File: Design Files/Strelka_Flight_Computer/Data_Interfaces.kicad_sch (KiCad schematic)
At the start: 9 parts, among them J2 Conn_01x04, J5 USB_B_Micro, J6 USB_B_Micro, U7 USBLC6-2SC6, U8 USBLC6-2SC6, U9 CP2102N-Axx-xQFN28

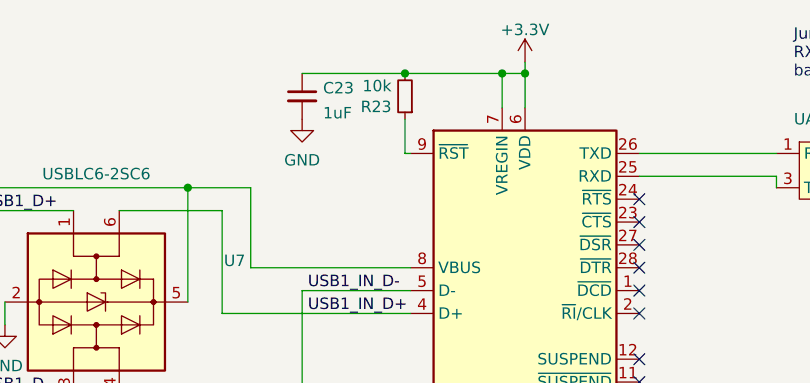
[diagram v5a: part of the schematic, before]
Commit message: Added motor driver to power board
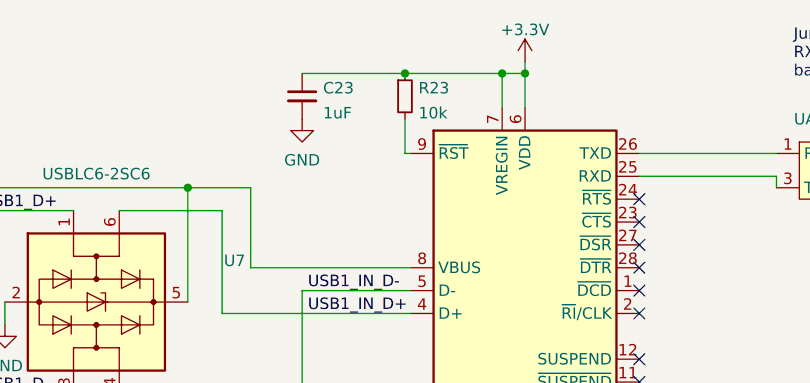
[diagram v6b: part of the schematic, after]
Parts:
- removed R23: 10k, Resistor_SMD:R_0603_1608Metric_Pad0.98x0.95mm_HandSolder, symbol Nebula-rescue:R_Small-Device-H7_FlightComputer-rescue
- added R23: 10k, Resistor_SMD:R_0603_1608Metric, symbol Device:R_Small
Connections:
- net +3V3: now also R23.1
- net at U9.9 (~{RST}): now also R23.2

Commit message: Creating BOM
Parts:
- removed J2: Conn_01x04, Connector_PinHeader_2.54mm:PinHeader_1x04_P2.54mm_Horizontal, symbol Connector_Generic:Conn_01x04
- added J2: SM04B-GHS-TB(LF)(SN)-, Footprints:JST_SM04B-GHS-TB(LF)(SN)-, symbol SM04B-GHS-TB_LF__SN_-:SM04B-GHS-TB(LF)(SN)-
- U7, U8: LCSC# (none) -> C2687116
- U9: LCSC# (none) -> C1550553
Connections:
- net +3V3: now also J2.4
- net GND: now also J2.3, J2.SH1 (SHIELD), J2.SH2 (SHIELD)
- net SWCLK: now also J2.1
- net SWDIO: now also J2.2
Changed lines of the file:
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@@
     (stroke (width 0) (type default) (color 0 0 0 0))
   )
-  (polyline (pts (xy 68.58 111.125) (xy 68.58 130.81))
+  (polyline (pts (xy 68.58 111.125) (xy 68.58 134.62))
     (stroke (width 0) (type default) (color 0 0 0 0))
   )
@@
     (stroke (width 0) (type default) (color 0 0 0 0))
   )
-  (wire (pts (xy 81.28 121.92) (xy 83.82 121.92))
+  (wire (pts (xy 77.47 121.92) (xy 83.82 121.92))
     (stroke (width 0) (type default) (color 0 0 0 0))
   )
@@
     (stroke (width 0) (type default) (color 0 0 0 0))
   )
-  (polyline (pts (xy 104.14 130.81) (xy 68.58 130.81))
+  (polyline (pts (xy 104.14 134.62) (xy 68.58 134.62))
     (stroke (width 0) (type default) (color 0 0 0 0))
   )
@@
     (stroke (width 0) (type default) (color 0 0 0 0))
   )
+  (wire (pts (xy 77.47 129.54) (xy 83.82 129.54))
+    (stroke (width 0) (type default) (color 0 0 0 0))
+  )
   (wire (pts (xy 212.09 30.48) (xy 222.885 30.48))
     (stroke (width 0) (type default) (color 0 0 0 0))
@@
     (stroke (width 0) (type default) (color 0 0 0 0))
   )
-  (wire (pts (xy 71.12 116.84) (xy 83.82 116.84))
-    (stroke (width 0) (type default) (color 0 0 0 0))
-  )
   (wire (pts (xy 187.96 85.09) (xy 187.96 97.79))
     (stroke (width 0) (type default) (color 0 0 0 0))
@@
     (stroke (width 0) (type default) (color 0 0 0 0))
   )
-  (polyline (pts (xy 104.14 111.125) (xy 104.14 130.81))
+  (polyline (pts (xy 104.14 111.125) (xy 104.14 134.62))
     (stroke (width 0) (type default) (color 0 0 0 0))
   )
@@
   )
   (wire (pts (xy 194.945 52.07) (xy 212.725 52.07))
+    (stroke (width 0) (type default) (color 0 0 0 0))
+  )
+  (wire (pts (xy 81.28 116.84) (xy 83.82 116.84))
     (stroke (width 0) (type default) (color 0 0 0 0))
   )
@@
     (effects (font (size 1.27 1.27)) (justify left bottom))
   )
-  (hierarchical_label "SWCLK" (shape input) (at 81.28 119.38 180)
+  (hierarchical_label "SWCLK" (shape input) (at 81.28 116.84 180)
     (effects (font (size 1.27 1.27)) (justify right))
   )
-  (hierarchical_label "SWDIO" (shape input) (at 81.28 121.92 180)
+  (hierarchical_label "SWDIO" (shape input) (at 81.28 119.38 180)
     (effects (font (size 1.27 1.27)) (justify right))
   )
@@
       (effects (font (size 1.27 1.27)) hide)
     )
+    (property "LCSC#" "C2687116" (id 4) (at 177.8 55.88 90)
+      (effects (font (size 1.27 1.27)) hide)
+    )
     (pin "1")
     (pin "2")
@@
     (pin "6")
   )
-  (symbol (lib_id "power:GND") (at 71.12 116.84 0) (unit 1)
+  (symbol (lib_id "power:GND") (at 77.47 121.92 0) (unit 1)
     (in_bom yes) (on_board yes)
-    (property "Reference" "#PWR0156" (id 0) (at 71.12 123.19 0)
-      (effects (font (size 1.27 1.27)) hide)
-    )
-    (property "Value" "GND" (id 1) (at 71.12 120.7676 0))
-    (property "Footprint" "" (id 2) (at 71.12 116.84 0)
-      (effects (font (size 1.27 1.27)) hide)
-    )
-    (property "Datasheet" "" (id 3) (at 71.12 116.84 0)
+    (property "Reference" "#PWR0156" (id 0) (at 77.47 128.27 0)
+      (effects (font (size 1.27 1.27)) hide)
+    )
+    (property "Value" "GND" (id 1) (at 77.47 125.8476 0))
+    (property "Footprint" "" (id 2) (at 77.47 121.92 0)
+      (effects (font (size 1.27 1.27)) hide)
+    )
+    (property "Datasheet" "" (id 3) (at 77.47 121.92 0)
       (effects (font (size 1.27 1.27)) hide)
     )
@@
     )
     (property "Datasheet" "" (id 3) (at 167.64 100.33 0)
+      (effects (font (size 1.27 1.27)) hide)
+    )
+    (pin "1")
+  )
+  (symbol (lib_id "power:GND") (at 77.47 129.54 0) (unit 1)
+    (in_bom yes) (on_board yes)
+    (property "Reference" "#PWR0112" (id 0) (at 77.47 135.89 0)
+      (effects (font (size 1.27 1.27)) hide)
+    )
+    (property "Value" "GND" (id 1) (at 77.47 133.4676 0))
+    (property "Footprint" "" (id 2) (at 77.47 129.54 0)
+      (effects (font (size 1.27 1.27)) hide)
+    )
+    (property "Datasheet" "" (id 3) (at 77.47 129.54 0)
       (effects (font (size 1.27 1.27)) hide)
     )
@@
       (effects (font (size 1.27 1.27)) hide)
     )
+    (property "LCSC#" "C2687116" (id 4) (at 177.8 97.79 90)
+      (effects (font (size 1.27 1.27)) hide)
+    )
     (pin "1")
     (pin "2")
@@
     (pin "6")
   )
-  (symbol (lib_id "Connector_Generic:Conn_01x04") (at 88.9 119.38 0) (unit 1)
-    (in_bom yes) (on_board yes) (fields_autoplaced)
-    (property "Reference" "J2" (id 0) (at 91.44 119.3799 0)
-      (effects (font (size 1.27 1.27)) (justify left))
-    )
-    (property "Value" "Conn_01x04" (id 1) (at 91.44 121.9199 0)
-      (effects (font (size 1.27 1.27)) (justify left))
-    )
-    (property "Footprint" "Connector_PinHeader_2.54mm:PinHeader_1x04_P2.54mm_Horizontal" (id 2) (at 88.9 119.38 0)
-      (effects (font (size 1.27 1.27)) hide)
-    )
-    (property "Datasheet" "~" (id 3) (at 88.9 119.38 0)
-      (effects (font (size 1.27 1.27)) hide)
-    )
-    (pin "1")
-    (pin "2")
-    (pin "3")
-    (pin "4")
-  )
   (symbol (lib_id "power:VBUS") (at 160.02 85.09 0) (unit 1)
     (in_bom yes) (on_board yes) (fields_autoplaced)
@@
     (pin "1")
   )
+  (symbol (lib_id "SM04B-GHS-TB_LF__SN_-:SM04B-GHS-TB(LF)(SN)-") (at 93.98 121.92 0) (unit 1)
+    (in_bom yes) (on_board yes) (fields_autoplaced)
+    (property "Reference" "J2" (id 0) (at 100.33 121.9199 0)
+      (effects (font (size 1.27 1.27)) (justify left))
+    )
+    (property "Value" "SM04B-GHS-TB(LF)(SN)-" (id 1) (at 100.33 124.4599 0)
+      (effects (font (size 1.27 1.27)) (justify left))
+    )
+    (property "Footprint" "Footprints:JST_SM04B-GHS-TB(LF)(SN)-" (id 2) (at 93.98 121.92 0)
+      (effects (font (size 1.27 1.27)) (justify left bottom) hide)
+    )
+    (property "Datasheet" "https://datasheet.lcsc.com/lcsc/1810261120_JST-Sales-America-SM04B-GHS-TB-LF-SN_C189895.pdf" (id 3) (at 93.98 121.92 0)
+      (effects (font (size 1.27 1.27)) (justify left bottom) hide)
+    )
+    (property "LCSC#" "C189895" (id 4) (at 93.98 121.92 0)
+      (effects (font (size 1.27 1.27)) hide)
+    )
+    (pin "1")
+    (pin "2")
+    (pin "3")
+    (pin "4")
+    (pin "SH1")
+    (pin "SH2")
+  )
   (symbol (lib_id "power:GND") (at 225.425 100.33 0) (unit 1)
     (in_bom yes) (on_board yes) (fields_autoplaced)
@@
       (effects (font (size 1.27 1.27)) hide)
     )
+    (property "LCSC#" "C1550553" (id 4) (at 225.425 67.31 0)
+      (effects (font (size 1.27 1.27)) hide)
+    )

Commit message: redo placement
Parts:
- removed C23: 1uF, Capacitor_SMD:C_0603_1608Metric_Pad1.08x0.95mm_HandSolder, symbol Device:C_Small
- removed J5: USB_B_Micro, Connector_USB:USB_Micro-B_Molex-105017-0001, symbol Connector:USB_B_Micro
- removed JP1: UART_Switch, Footprints:UART_Switch, symbol UART_Switch:UART_Switch
- removed R23: 10k, Resistor_SMD:R_0603_1608Metric, symbol Device:R_Small
- removed U7: USBLC6-2SC6, Package_TO_SOT_SMD:SOT-23-6, symbol Power_Protection:USBLC6-2SC6
- removed U9: CP2102N-Axx-xQFN28, Package_DFN_QFN:QFN-28-1EP_5x5mm_P0.5mm_EP3.35x3.35mm, symbol Interface_USB:CP2102N-Axx-xQFN28
- added TP1, TP2: TestPoint, TestPoint:TestPoint_Pad_2.0x2.0mm, symbol Connector:TestPoint
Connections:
- new net RX_PAD: TP1.1
- new net TX_PAD: TP2.1
- no-connect marks 20 -> 1
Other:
- note removed: "Give USB ports enough separation to connect multiple micro USBs at once"
- note removed: "Jumpers used if RX and TX are backwards"
- moved on the sheet: J6, U8
